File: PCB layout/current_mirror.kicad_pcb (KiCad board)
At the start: 2 copper layers, 78 x 67 mm, 21 parts, among them J1 12V INPUT, Q1 2N3904, Q2 2N3904

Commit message: Fit measured trimmer geometry and retain unverified pinout status
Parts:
- RV1: footprint Project:RV1_PENDING -> Project:RV1_D9_P8_Offset5_PINOUT_UNVERIFIED
- moved RV1 4.00 mm to (49.0, 38.0)
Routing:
- net /BASE: track 47.5 -> 49.9 mm
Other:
- board text added: "P1 - VERIFY RV1 WIPER"
- board text added: "RV1 PINOUT UNVERIFIED"
- board text removed: "P0 - NOT FOR FABRICATION"
- board text removed: "RV1 SPACE RESERVED"

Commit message: Replace trimmer with fixed 120 ohm resistor and validate P2 PCB
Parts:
- removed RV1: 500R TRIM / set ~119.8R, Project:RV1_D9_P8_Offset5_PINOUT_UNVERIFIED
- added R7: 120R, Project:R7_ETCH, F.Cu at (45.0, 38.0)
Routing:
- net /BASE: track 49.9 -> 47.5 mm
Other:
- board text added: "P2 - FIXED R7 120R"
- board text removed: "P1 - VERIFY RV1 WIPER"
- board text removed: "RV1 PINOUT UNVERIFIED"

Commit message: Sync PCB values with revised LTspice schematic and validate P3
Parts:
- C1: value 100n / >=25V -> 1.33n / >=25V
- J1: value 12V INPUT -> 9.8V INPUT
- R2: value 620R (LT Rs) -> 662R (LT Rs)
- R7: value 120R -> 120R (117.6R measured)
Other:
- board text added: "+9.8V"
- board text added: "CURRENT MIRROR"
- board text added: "P3 - SOURCE VALUES SYNC"
- board text removed: "+12V"
- board text removed: "5 mA CURRENT MIRROR"
- board text removed: "P2 - FIXED R7 120R"
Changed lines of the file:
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@@
 			)
 		)
-		(property "Value" "620R (LT Rs)"
+		(property "Value" "662R (LT Rs)"
 			(at 3.81 2.37 270)
 			(layer "F.Fab")
@@
 			)
 		)
-		(property "Value" "12V INPUT"
+		(property "Value" "9.8V INPUT"
 			(at 0 4.92 0)
 			(layer "F.Fab")
@@
 			)
 		)
-		(property "Value" "120R"
+		(property "Value" "120R (117.6R measured)"
 			(at 3.81 2.37 0)
 			(layer "F.Fab")
@@
 			)
 		)
-		(property "Value" "100n / >=25V"
+		(property "Value" "1.33n / >=25V"
 			(at 2.5 2.5 0)
 			(layer "F.Fab")
@@
 		(layer "Edge.Cuts")
 	)
-	(gr_text "+12V"
+	(gr_text "+9.8V"
 		(at 8 7.5 0)
 		(layer "F.SilkS")
@@
 		)
 	)
-	(gr_text "P2 - FIXED R7 120R"
+	(gr_text "P3 - SOURCE VALUES SYNC"
 		(at 42 68 0)
 		(layer "F.SilkS")
@@
 		)
 	)
-	(gr_text "5 mA CURRENT MIRROR"
+	(gr_text "CURRENT MIRROR"
 		(at 43 5.7 0)
 		(layer "F.SilkS")

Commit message: Add isolated dual current mirror panel with measurement headers
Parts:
- removed TP1: GND, Project:TP1_ETCH
- removed TP2: VIN, Project:TP2_ETCH
- removed TP3: VCC / LOAD+, Project:TP3_ETCH
- removed TP4: VA, Project:TP4_ETCH
- removed TP5: BASE, Project:TP5_ETCH
- removed TP6: OUT / LOAD-, Project:TP6_ETCH
- added J2: RLOAD VOLTAGE, Project:J2_ETCH, F.Cu at (73.0, 28.0)
- added J3: Q1 BASE-EMITTER, Project:J3_ETCH, F.Cu at (40.0, 45.0)
- added J4: Q2 BASE-EMITTER, Project:J4_ETCH, F.Cu at (73.0, 48.0)
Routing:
- net /BASE: track 47.5 -> 96.0 mm
- net /VA: track 38.9 -> 68.2 mm
- net /VCC: track 76.0 -> 94.0 mm
- net /E2: track 8.00 -> 25.5 mm
- net /VIN: track 22.0 -> 8.00 mm
- net /OUT: track 42.7 -> 28.9 mm
- net /E1: track 8.00 -> 15.5 mm
- net /GND: track 176.0 -> 175.5 mm
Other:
- board text added: "+"
- board text added: "-"
- board text added: "B"
- board text added: "E"
- board text added: "P4 - MEASUREMENT HEADERS"
- board text added: "Q1 VBE"
- board text added: "Q2 VBE"
- board text added: "RLOAD"
- board text removed: "BASE"
- board text removed: "OUT"
- board text removed: "P3 - SOURCE VALUES SYNC"
- board text removed: "VA"
- board text removed: "VCC"

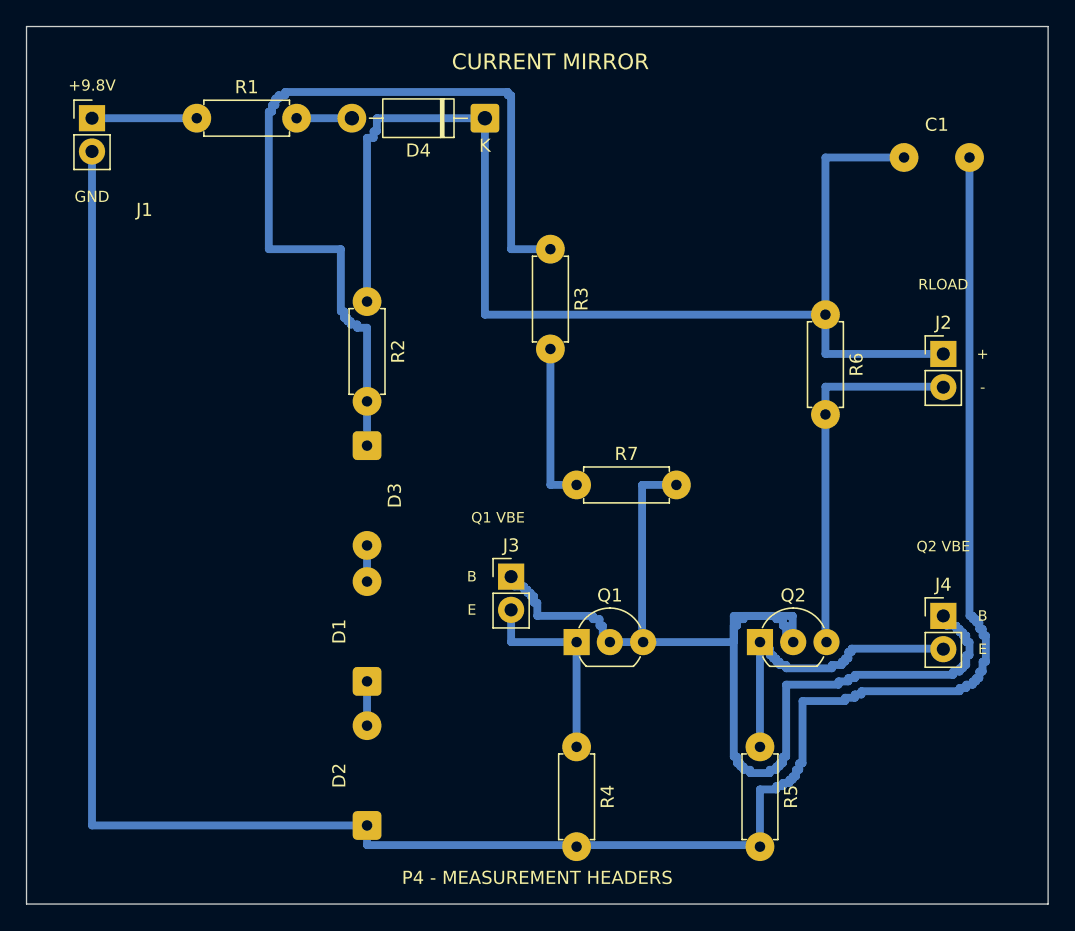
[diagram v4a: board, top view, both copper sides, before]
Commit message: Increase soldering clearance on both current mirror copies
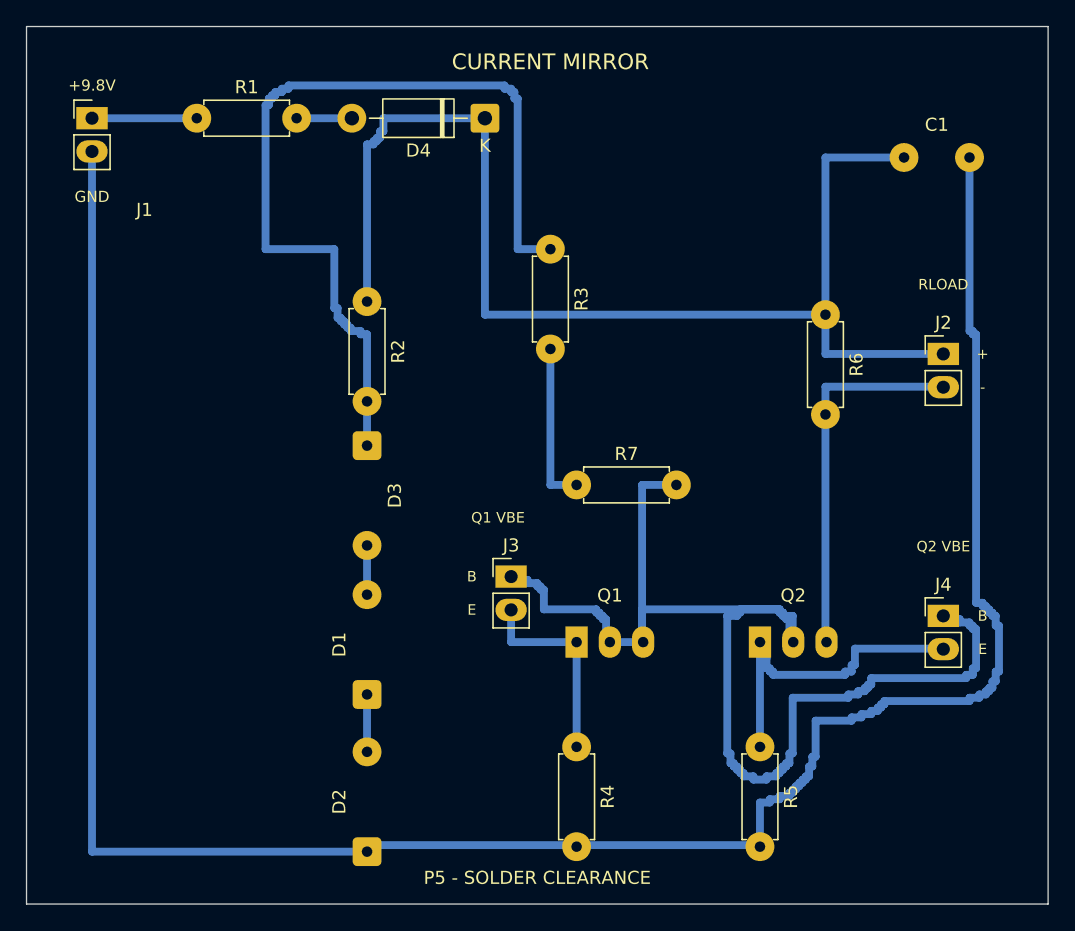
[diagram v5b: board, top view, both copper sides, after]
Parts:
- moved D2 2.00 mm to (29.0, 66.0)
- moved D1 1.00 mm to (29.0, 54.0)
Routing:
- net /BASE: track 96.0 -> 101.0 mm
- net /GND: track 175.5 -> 178.5 mm
- net /VA: track 68.2 -> 69.7 mm
- net /ZD_A: track 3.24 -> 4.24 mm
- net /E2: track 25.5 -> 26.5 mm
- net /D12: track 3.62 -> 4.62 mm
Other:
- board text added: "P5 - SOLDER CLEARANCE"
- board text removed: "P4 - MEASUREMENT HEADERS"

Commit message: Restore P6 PCB layout and retain centre-cut manufacturing setup
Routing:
- net /VA: track 69.7 -> 22.3 mm
- net /BASE: track 101.0 -> 56.9 mm
- net /GND: track 178.5 -> 153.9 mm
- net /VCC: track 94.0 -> 74.7 mm
- net /OUT: track 28.9 -> 27.3 mm
- net /E1: track 15.5 -> 14.0 mm
- net /TRIM_TOP: track 12.6 -> 11.3 mm
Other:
- board text added: "P6 - STRAIGHT ROUTES"
- board text removed: "P5 - SOLDER CLEARANCE"
